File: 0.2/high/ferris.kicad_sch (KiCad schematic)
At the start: 102 parts, among them J1 TYPE-C-31-M-12, K0_0 KEYSW, K0_1 KEYSW, K0_2 KEYSW, K0_3 KEYSW, K0_4 KEYSW, K0_5 KEYSW, K0_6 KEYSW, K0_7 KEYSW, K0_8 KEYSW, K0_9 KEYSW, K1_0 KEYSW, K1_1 KEYSW, K1_2 KEYSW, K1_3 KEYSW, K1_4 KEYSW, K1_5 KEYSW, K1_6 KEYSW, K1_7 KEYSW, K1_8 KEYSW, K1_9 KEYSW, K2_0 KEYSW, K2_1 KEYSW, K2_2 KEYSW, K2_3 KEYSW, K2_4 KEYSW, K2_5 KEYSW, K2_6 KEYSW, K2_7 KEYSW, K2_8 KEYSW, K2_9 KEYSW, K3_3 KEYSW, K3_4 KEYSW, K3_5 KEYSW, K3_6 KEYSW, Q1 PDTC123JT,215, SW1 B3U-1000P, U1 STM32F072CBT6, U2 MCP23017-E/SO, U3 MCP1700T-3302E/TT, U4 SRV05-4

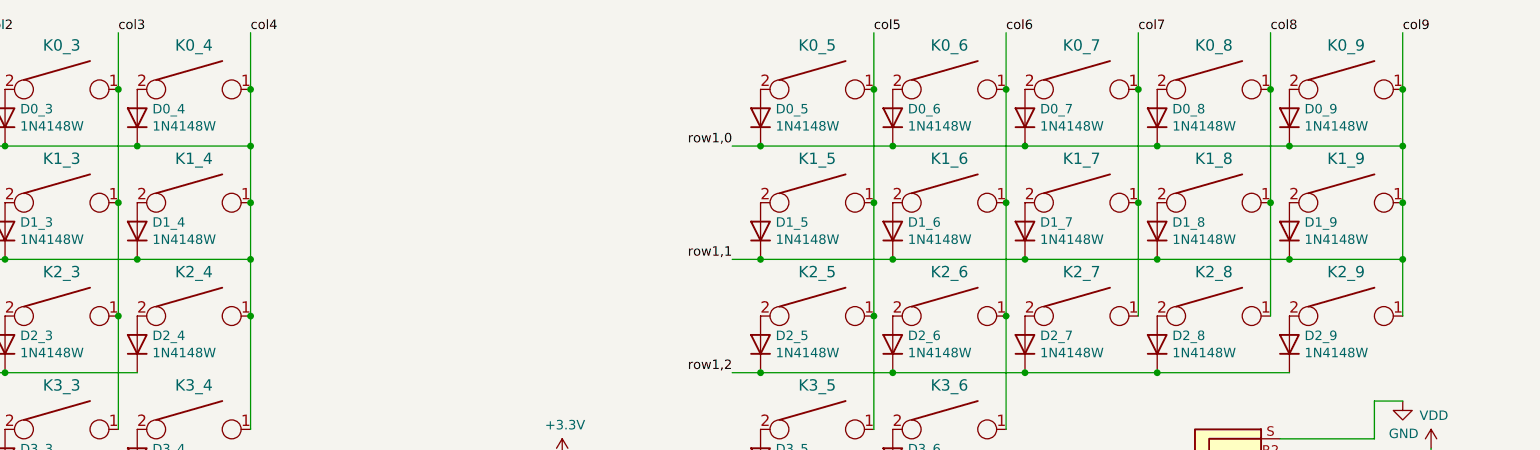
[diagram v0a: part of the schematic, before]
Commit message: Again, fix schematic bug connecting rows directly to rightmost column
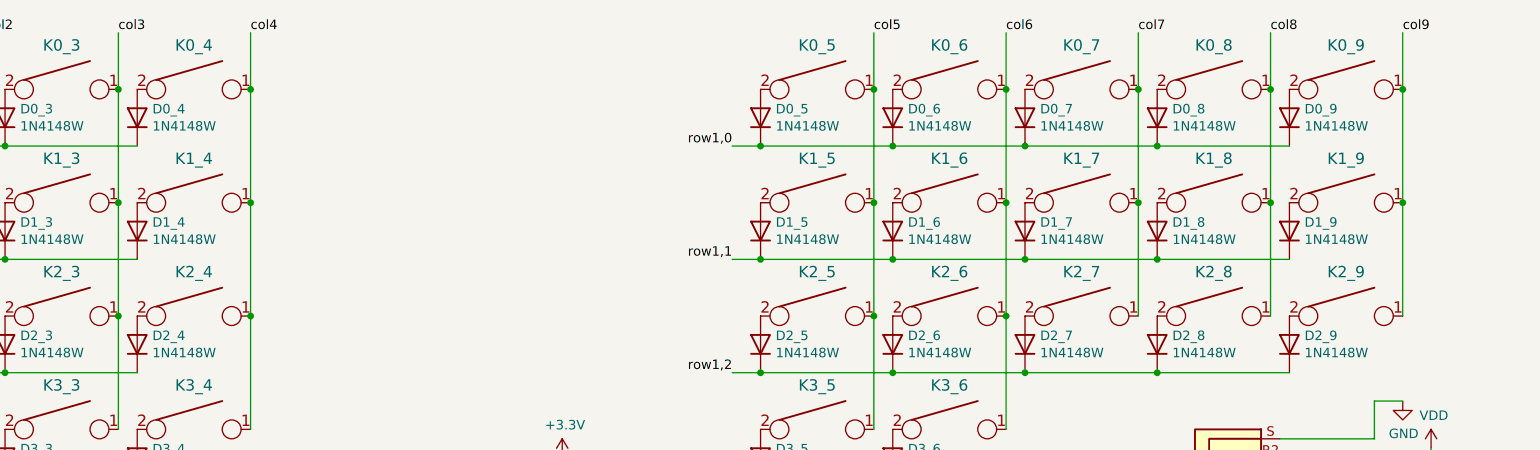
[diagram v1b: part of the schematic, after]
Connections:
- net col4: no longer D0_0.1 (K), D0_1.1 (K), D0_2.1 (K), D0_3.1 (K), D0_4.1 (K), D1_0.1 (K), D1_1.1 (K), D1_2.1 (K), D1_3.1 (K), D1_4.1 (K), U1.42 (PB6), U1.43 (PB7)
- net col9: no longer D0_5.1 (K), D0_6.1 (K), D0_7.1 (K), D0_8.1 (K), D0_9.1 (K), D1_5.1 (K), D1_6.1 (K), D1_7.1 (K), D1_8.1 (K), D1_9.1 (K), U2.1 (GPB0), U2.2 (GPB1)
- new net row0,0: D0_0.1 (K), D0_1.1 (K), D0_2.1 (K), D0_3.1 (K), D0_4.1 (K), U1.43 (PB7)
- new net row0,1: D1_0.1 (K), D1_1.1 (K), D1_2.1 (K), D1_3.1 (K), D1_4.1 (K), U1.42 (PB6)
- new net row1,0: D0_5.1 (K), D0_6.1 (K), D0_7.1 (K), D0_8.1 (K), D0_9.1 (K), U2.1 (GPB0)
- new net row1,1: D1_5.1 (K), D1_6.1 (K), D1_7.1 (K), D1_8.1 (K), D1_9.1 (K), U2.2 (GPB1)

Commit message: Again, initiate reversible
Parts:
- removed C12, C13: 0.1uF, Capacitor_SMD:C_0805_2012Metric_Pad1.15x1.40mm_HandSolder, symbol Device:C_Small
- removed D0_5, D0_6, D0_7, D0_8, D0_9, D1_5, D1_6, D1_7, D1_8, D1_9, D2_5, D2_6, D2_7, D2_8, D2_9, D3_5, D3_6: 1N4148W, Diode_SMD:D_SOD-123, symbol Device:D
- removed Jack1: PJ-320A, kbd:TRRS-PJ-320A, symbol Connector:AudioJack4
- removed K0_5, K0_6, K0_7, K0_8, K0_9, K1_5, K1_6, K1_7, K1_8, K1_9, K2_5, K2_6, K2_7, K2_8, K2_9, K3_5, K3_6: KEYSW, switches:MX, symbol keyboard_parts:KEYSW
- removed R6: 10kΩ, Resistor_SMD:R_0805_2012Metric_Pad1.15x1.40mm_HandSolder, symbol Device:R
- removed R7, R8: 4.7kΩ, Resistor_SMD:R_0805_2012Metric_Pad1.15x1.40mm_HandSolder, symbol Device:R
- removed U2: MCP23017-E/SO, Package_SO:SOIC-28W_7.5x17.9mm_P1.27mm, symbol Interface_Expansion:MCP23017_SO
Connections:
- no-connect marks 37 -> 28
